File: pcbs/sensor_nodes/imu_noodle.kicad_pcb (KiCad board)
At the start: 2 copper layers, 11 x 36 mm, 24 parts, among them P1 CONN_02X05, U1 PCA9615, U2 LTC4316, U3 BNO055

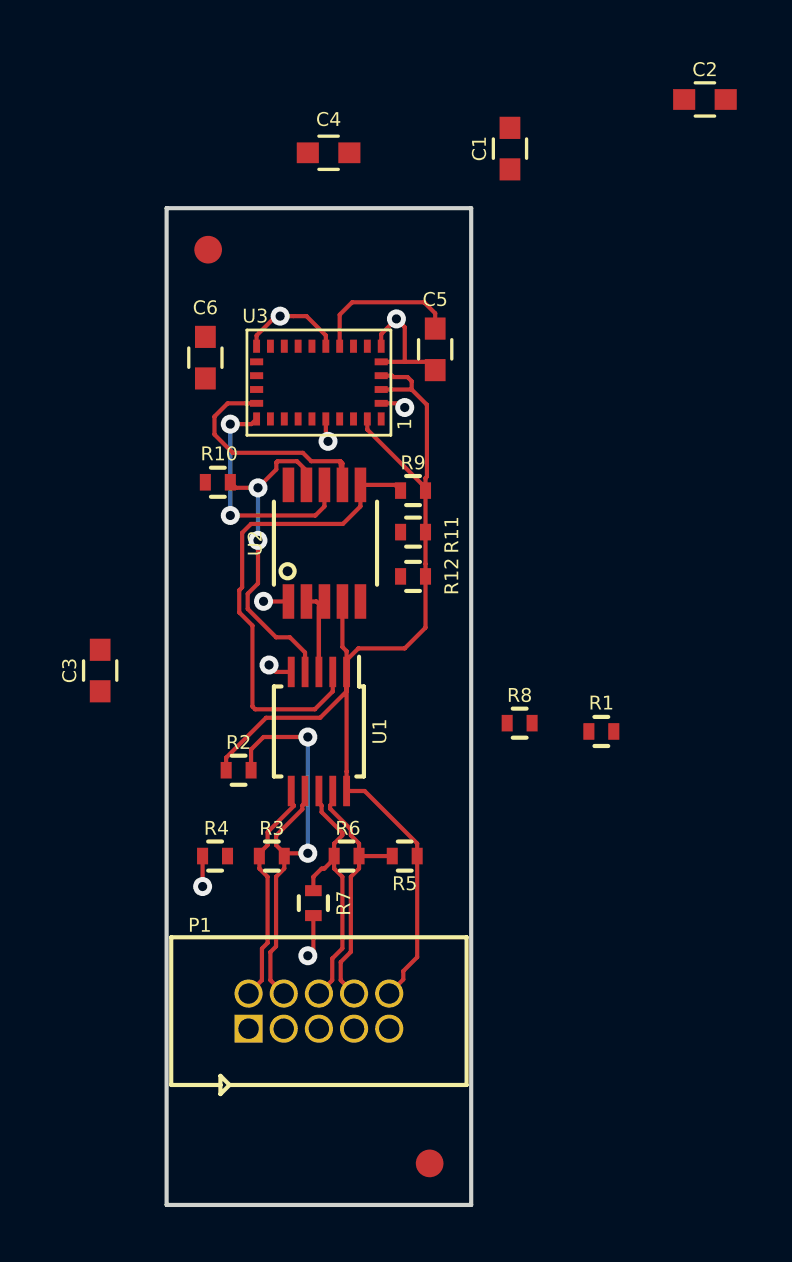
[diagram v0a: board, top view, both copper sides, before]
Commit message: added more caps; specified BOM components; finished first pass at layout
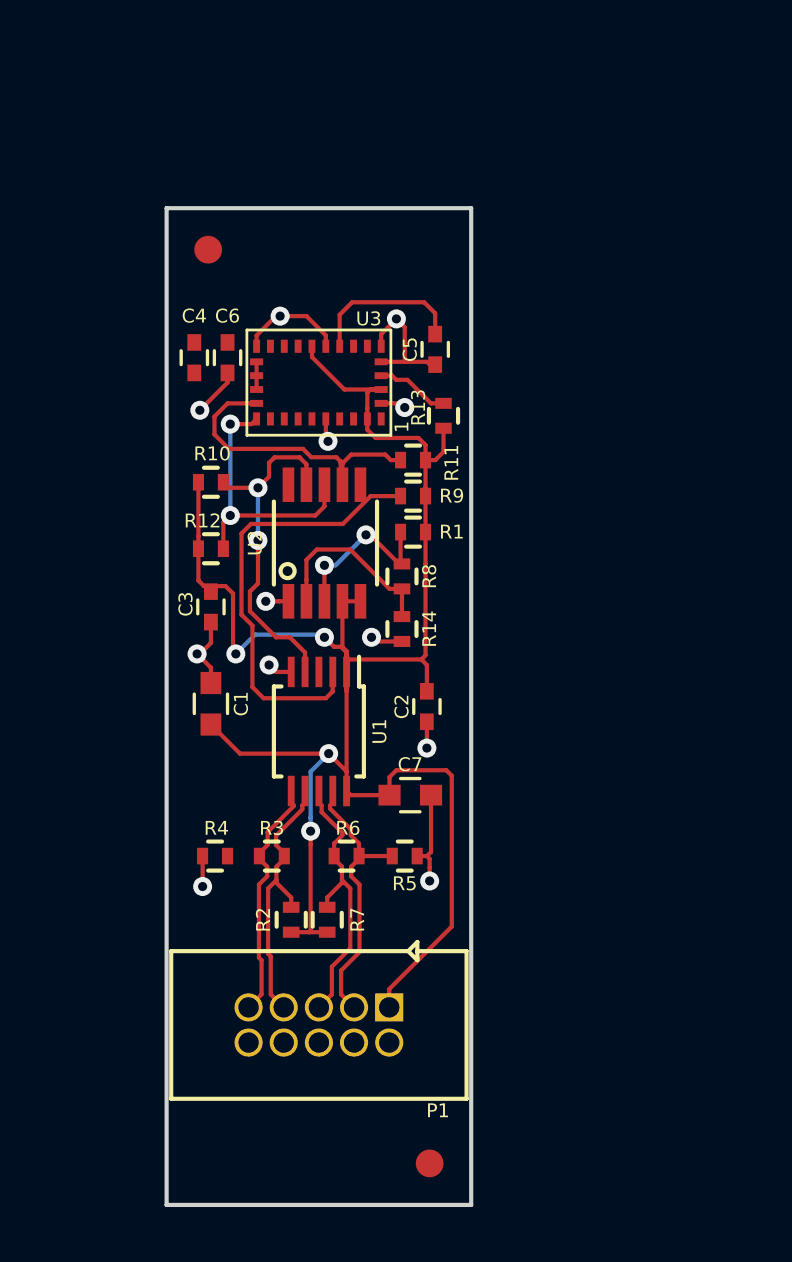
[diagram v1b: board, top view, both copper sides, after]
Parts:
- added C7: 1uF, Capacitors_SMD:C_0603, F.Cu at (145.3, 79.2)
- added R13: 10K, Resistors_SMD:R_0402, F.Cu at (146.5, 65.5)
- added R14: TBD, Resistors_SMD:R_0402, F.Cu at (145.0, 73.2)
- C2, C3, C4: footprint Capacitors_SMD:C_0603 -> Capacitors_SMD:C_0402
- C5, C6: value 100nF -> 0.1uF; footprint Capacitors_SMD:C_0603 -> Capacitors_SMD:C_0402
- moved C2 24.1 mm to (145.9, 76.0), turned to 90 degrees
- moved C1 22.8 mm to (138.1, 75.9), turned to 90 degrees
- moved R1 9.90 mm to (145.4, 69.7), turned to 180 degrees
- moved C4 8.85 mm to (137.5, 63.4), turned to 90 degrees
- moved R12 7.37 mm to (138.1, 70.3), turned to 0 degrees
- moved R8 6.79 mm to (145.0, 71.3), turned to 270 degrees
- moved R2 5.72 mm to (141.0, 83.7), turned to 90 degrees
- moved C3 4.61 mm to (138.1, 72.4)
- moved R11 2.60 mm to (145.4, 67.1)
- moved C6 0.80 mm to (138.7, 63.4)
- moved R7 0.78 mm to (142.3, 83.7)
- moved P1 0.50 mm to (142.0, 87.5), turned to 180 degrees
- moved R10 0.25 mm to (138.1, 67.9)
- moved R9 0.20 mm to (145.4, 68.4)
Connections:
- net Net-(R11-Pad2) renamed /t_scl
- net Net-(R12-Pad2) renamed /t_sda
- C2 pad 1: +3V3 -> GNDD
- C2 pad 2: GNDD -> +3V3
- P1 pad 1: Net-(P1-Pad1) -> +3V3
- P1 pad 10: +3V3 -> GNDD
- P1 pad 2: /DSCL0_N -> GNDD
- P1 pad 3: Net-(P1-Pad1) -> /DSDA0_N
- P1 pad 4: /DSCL0_P -> GNDD
- P1 pad 5: Net-(P1-Pad1) -> /DSDA0_P
- P1 pad 6: /DSDA0_P -> GNDD
- P1 pad 7: Net-(P1-Pad1) -> /DSCL0_P
- P1 pad 8: /DSDA0_N -> GNDD
- P1 pad 9: Net-(P1-Pad1) -> /DSCL0_N
- R1 pad 1: (no net) -> +3V3
- R1 pad 2: (no net) -> Net-(R1-Pad2)
- R5 pad 1: +3V3 -> GNDD
- R7 pad 2: GNDD -> +3V3
- R8 pad 1: (no net) -> Net-(R1-Pad2)
- R8 pad 2: (no net) -> Net-(R14-Pad1)
- U2 pad 2: (no net) -> Net-(R14-Pad1)
- U2 pad 3: (no net) -> Net-(R1-Pad2)
- U2 pad 5: (no net) -> +3V3
- U3 pad 4: +3V3 -> Net-(R13-Pad2)
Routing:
- net +3V3: track 41.2 -> 69.8 mm, vias 0 -> 4
- net GNDD: track 15.0 -> 24.3 mm, vias 8 -> 12
- net Net-(R14-Pad1): track 0.00 -> 6.69 mm
- net /DSCL0_P: track 16.5 -> 10.2 mm, vias 2 -> 0
- net Net-(R1-Pad2): track 0.00 -> 6.16 mm, vias 0 -> 2
- net (no net): track 5.57 -> 0.00 mm
- net Net-(R13-Pad2): track 0.00 -> 2.66 mm
- net /t_scl: track 9.06 -> 11.4 mm
- net SDA_CLASH: track 17.4 -> 15.9 mm
- net /t_sda: track 8.64 -> 9.94 mm
- net /DSDA0_N: track 9.46 -> 10.2 mm
- net SCL_CLASH: track 12.0 -> 12.6 mm
- added copper zone on B.Cu, net GNDD
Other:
- rule pad_to_mask_clearance: 0.2 -> 0.1

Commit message: finished node layout; passes drc
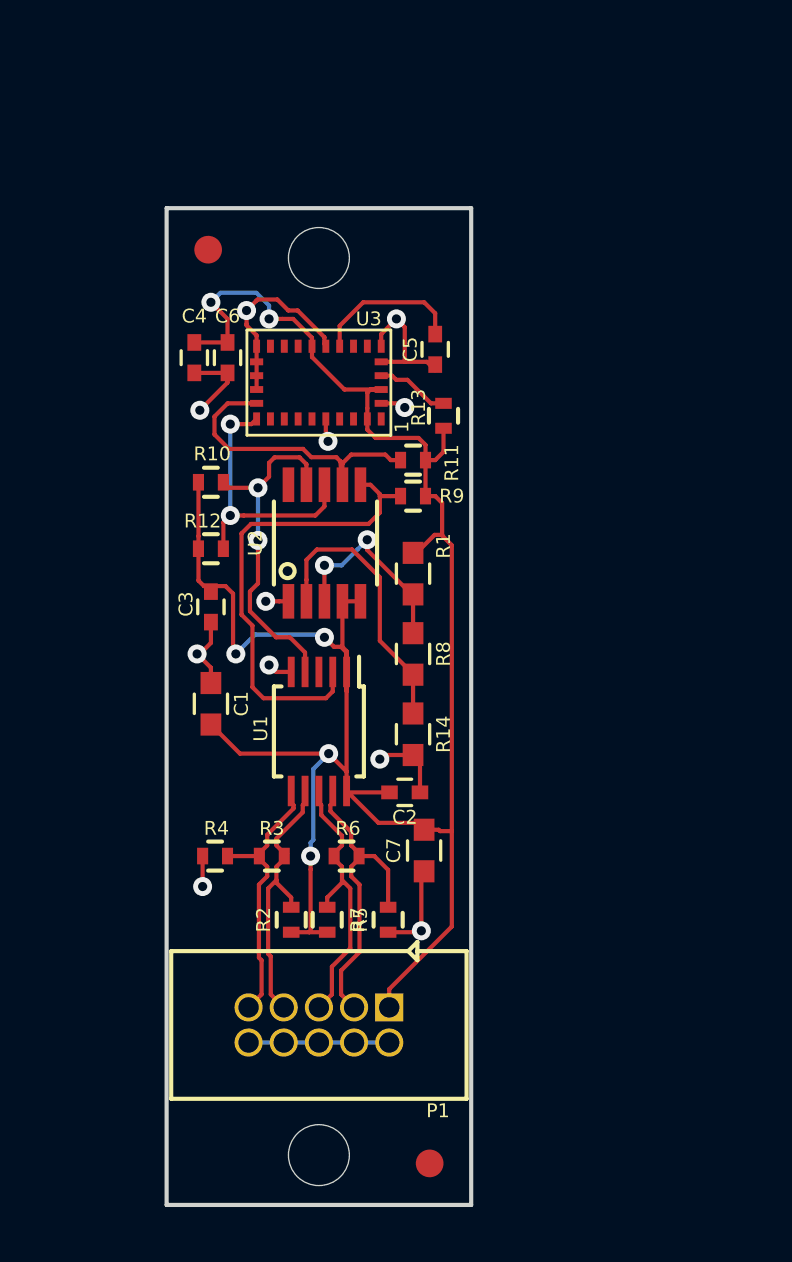
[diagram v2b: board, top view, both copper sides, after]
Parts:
- added REF**: MountingHole_2.2mm_M2_ISO14580, Mounting_Holes:MountingHole_2.2mm_M2_ISO14580, F.Cu at (142.0, 92.2)
- added REF**: MountingHole_2.2mm_M2_ISO14580, Mounting_Holes:MountingHole_2.2mm_M2_ISO14580, F.Cu at (142.0, 59.8)
- R1, R14, R8: footprint Resistors_SMD:R_0402 -> Capacitors_SMD:C_0603
- moved R14 3.82 mm to (145.4, 77.0)
- moved C2 3.20 mm to (145.1, 79.1), turned to 180 degrees
- moved R8 2.83 mm to (145.4, 74.1)
- moved R5 2.38 mm to (144.5, 83.7), turned to 90 degrees
- moved C7 2.06 mm to (145.8, 81.2), turned to 270 degrees
- moved R1 1.50 mm to (145.4, 71.2), turned to 270 degrees
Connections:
- U3 pad 1: Net-(U3-Pad1) -> (no net)
- U3 pad 12: Net-(U3-Pad1) -> (no net)
- U3 pad 13: Net-(U3-Pad1) -> (no net)
- U3 pad 21: Net-(U3-Pad1) -> (no net)
- U3 pad 22: Net-(U3-Pad1) -> (no net)
- U3 pad 23: Net-(U3-Pad1) -> (no net)
- U3 pad 24: Net-(U3-Pad1) -> (no net)
- U3 pad 7: Net-(U3-Pad1) -> (no net)
- U3 pad 8: Net-(U3-Pad1) -> (no net)
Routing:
- net +3V3: track 69.8 -> 81.2 mm, vias 4 -> 6
- net GNDD: track 24.3 -> 33.3 mm, vias 12 -> 11
- net Net-(R14-Pad1): track 6.69 -> 10.1 mm
- net /DSDA0_N: track 10.2 -> 11.6 mm
- net SDA_CLASH: track 15.9 -> 17.2 mm
- net Net-(R1-Pad2): track 6.16 -> 7.32 mm
- net /DSCL0_N: track 8.85 -> 9.99 mm

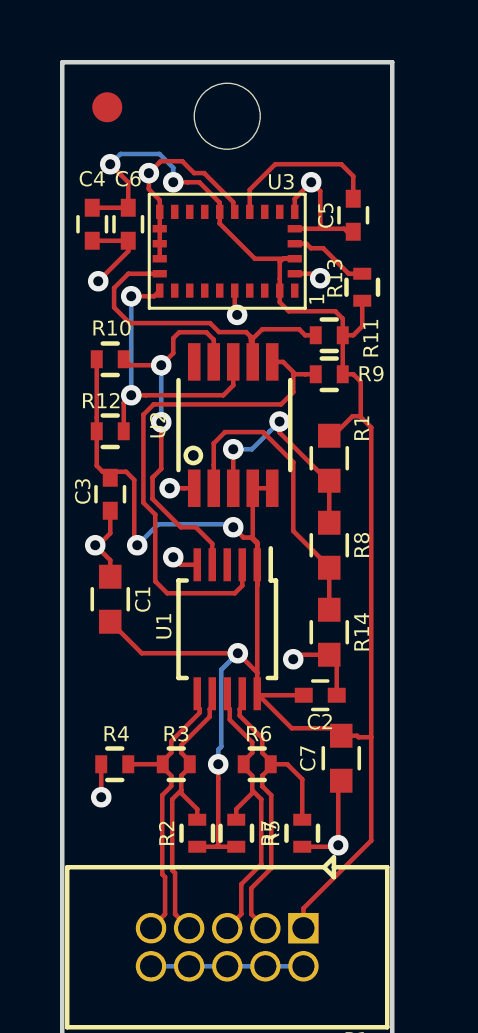
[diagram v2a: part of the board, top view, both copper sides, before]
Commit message: finished node sch and pcb; passes drc
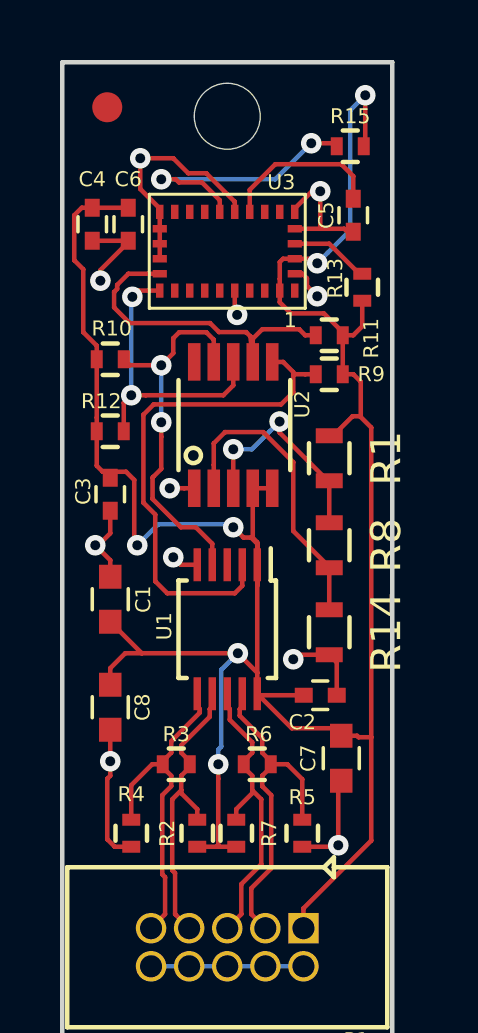
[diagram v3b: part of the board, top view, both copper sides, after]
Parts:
- added C8: 10uF, Capacitors_SMD:C_0603, F.Cu at (138.1, 79.5)
- added R15: 10K, Resistors_SMD:R_0402, F.Cu at (146.1, 60.8)
- R1, R14, R8: footprint Capacitors_SMD:C_0603 -> Resistors_SMD:R_0603
- R2, R4, R5, R7: value TBD -> 470
- R3, R6: value TBD -> 140
- moved R4 2.36 mm to (138.8, 83.7), turned to 270 degrees
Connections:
- U3 pad 11: +3V3 -> Net-(R15-Pad2)
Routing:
- net Net-(R15-Pad2): track 0.00 -> 9.02 mm, vias 0 -> 2
- net +3V3: track 81.2 -> 87.2 mm
- net GNDD: track 33.3 -> 37.4 mm
- net /DSCL0_N: track 9.99 -> 11.3 mm

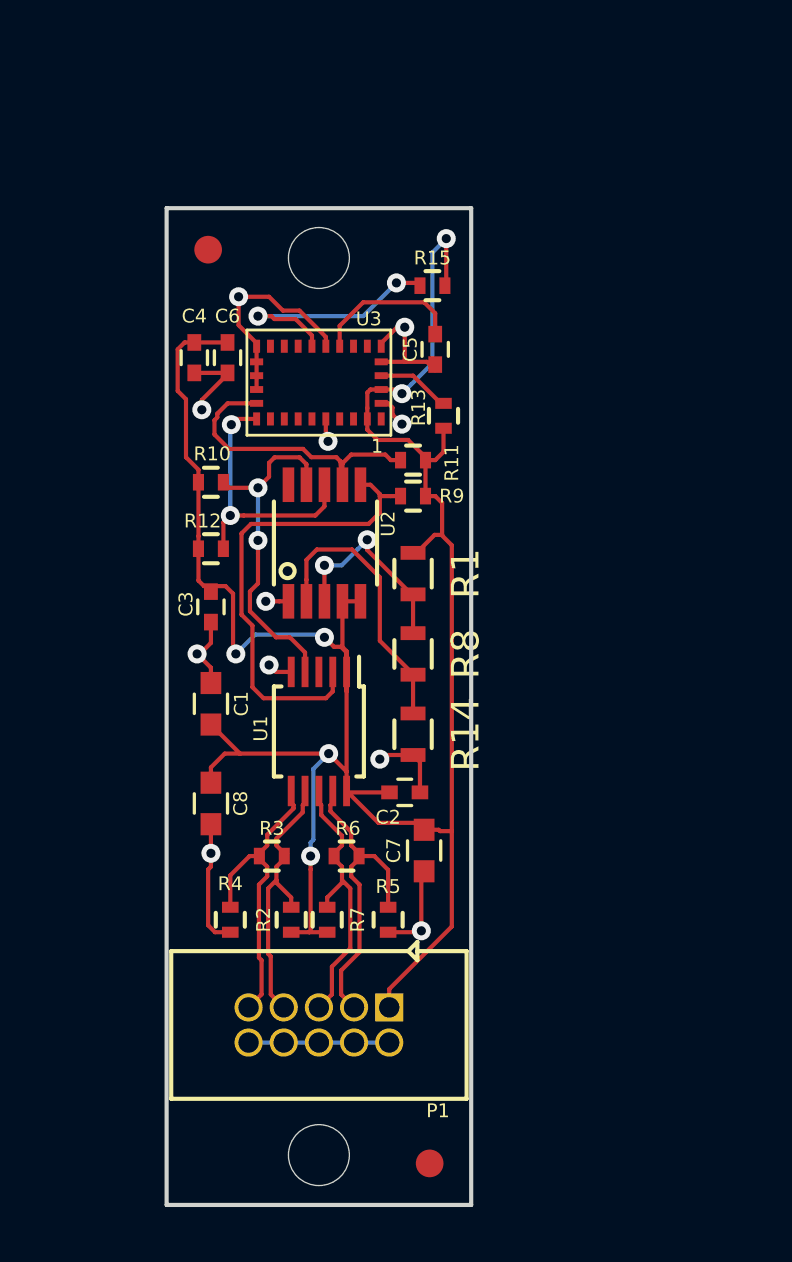
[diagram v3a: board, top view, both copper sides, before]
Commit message: added beginnings of a bno055 driver
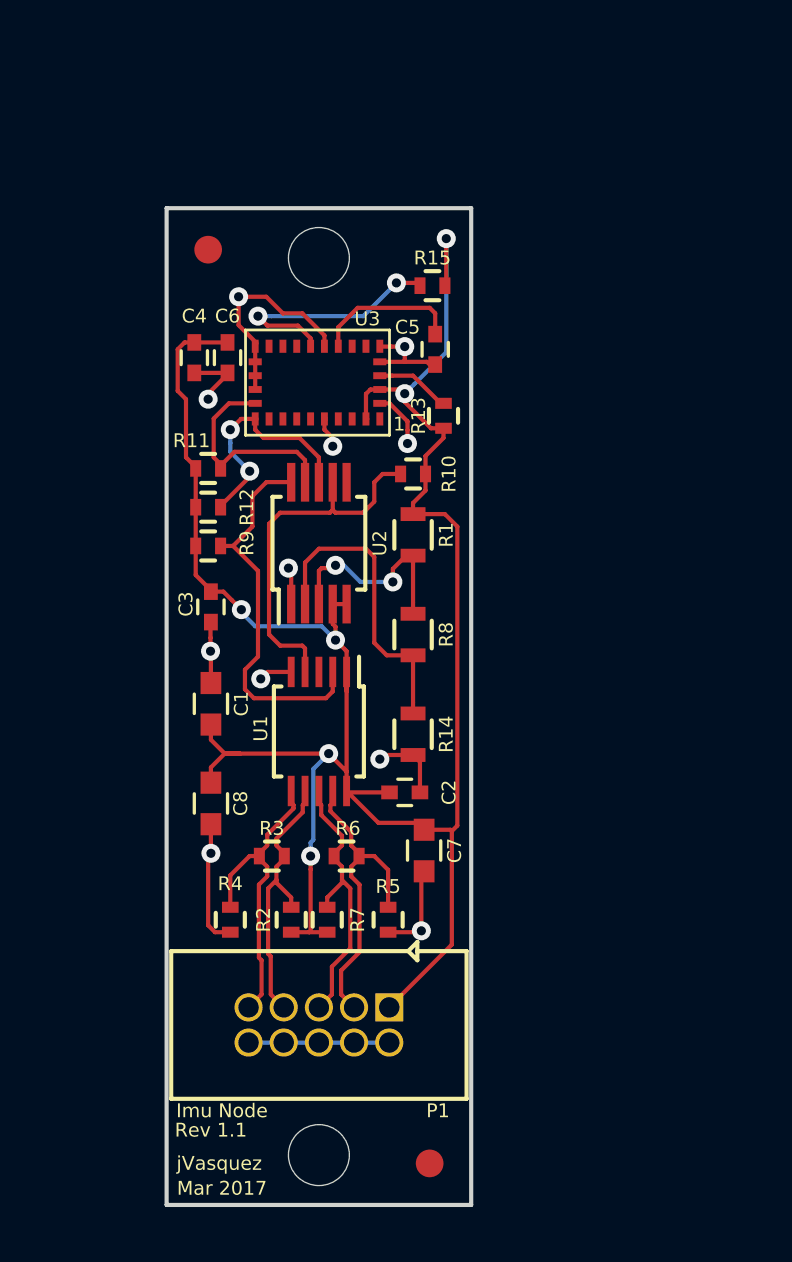
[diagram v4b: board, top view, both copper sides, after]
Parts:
- U2: footprint double_jump_electric_component_library:MSOP-10 -> Housings_SSOP:MSOP-10_3x3mm_Pitch0.5mm
- moved R9 7.62 mm to (138.0, 70.2), turned to 0 degrees
- moved R11 7.41 mm to (138.0, 67.4), turned to 0 degrees
- moved R10 7.31 mm to (145.4, 67.6), turned to 180 degrees
- moved R12 1.50 mm to (138.0, 68.8)
- moved R1 1.40 mm to (145.4, 69.8)
- moved R8 0.70 mm to (145.4, 73.4)
- moved U2 0.20 mm to (142.0, 70.1)
- moved U3 0.05 mm to (141.9, 64.3)
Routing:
- net +3V3: track 87.2 -> 83.6 mm
- net /t_scl: track 11.4 -> 8.18 mm
- net SDA_CLASH: track 17.2 -> 14.1 mm
- net /t_sda: track 9.91 -> 8.64 mm
- net Net-(R14-Pad1): track 10.1 -> 11.1 mm
- net SCL_CLASH: track 12.6 -> 13.3 mm, vias 2 -> 0
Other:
- board text added: "Imu Node"
- board text added: "Mar 2017"
- board text added: "Rev 1.1"
- board text added: "jVasquez"
